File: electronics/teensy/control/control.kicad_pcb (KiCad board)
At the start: 2 copper layers, 100 x 100 mm, 154 parts, among them J1 Vin 24V, J10 Z_MAX, J11 OTHER_2, J12 Stepper X1, J13 Stepper X2, J14 Stepper X1, J15 Stepper X1, J16 DC Motor Vin 24V, J18 DC Motor, J2 Vout 5V, J20 DC Motor Vin 24V, J21 DC Motor, J22 SPINDLE_BLDC_CONTROLLER, J23 USB_B, J24 EXT, J25 EXT, J3 Vout 3.3V, J4 X_MIN, J5 Y_MIN, J6 Z_MIN, J7 OTHER 1, J8 X_MAX, J9 Y_MAX, Q1 TK1R4S04PB, Q3 TK1R4S04PB, Q4 SI2301CDS-T1-E3, U1 MIC4684, U10 MOCD217R2M, U11 MOCD217R2M, U12 MOCD217R2M, U13 MOCD217R2M, U14 TS912, U15 MOCD217R2M, U16 Cetus_J1B1211CCD, U17 CY7C64225, U18 LM810M3-4.63, U19 Teensy_4.1, U2 AP7354-33W5-7, U3 AZ1117IH-3.3TRG1, U4 SN74LVC14ADRG3, U5 SN74LVC14ADRG3, U6 MOCD217R2M, U7 MOCD217R2M, U8 MOCD217R2M, U9 MOCD217R2M

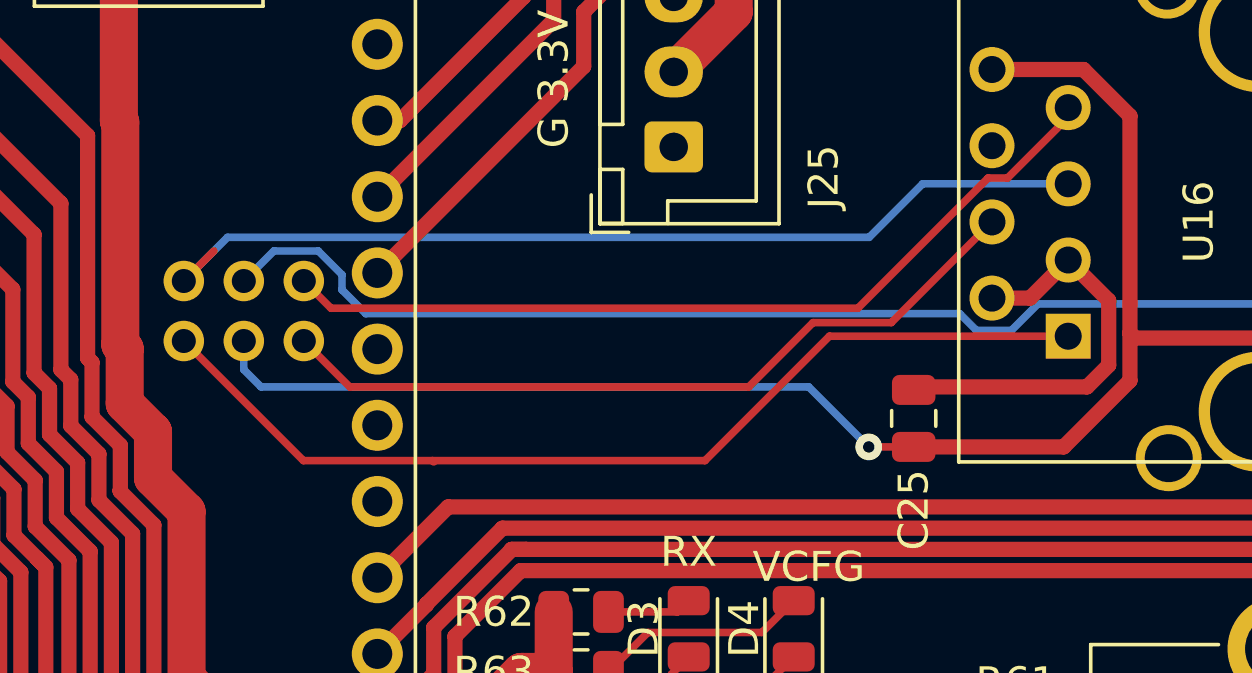
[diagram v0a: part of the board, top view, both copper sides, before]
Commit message: Add core classes and functions.
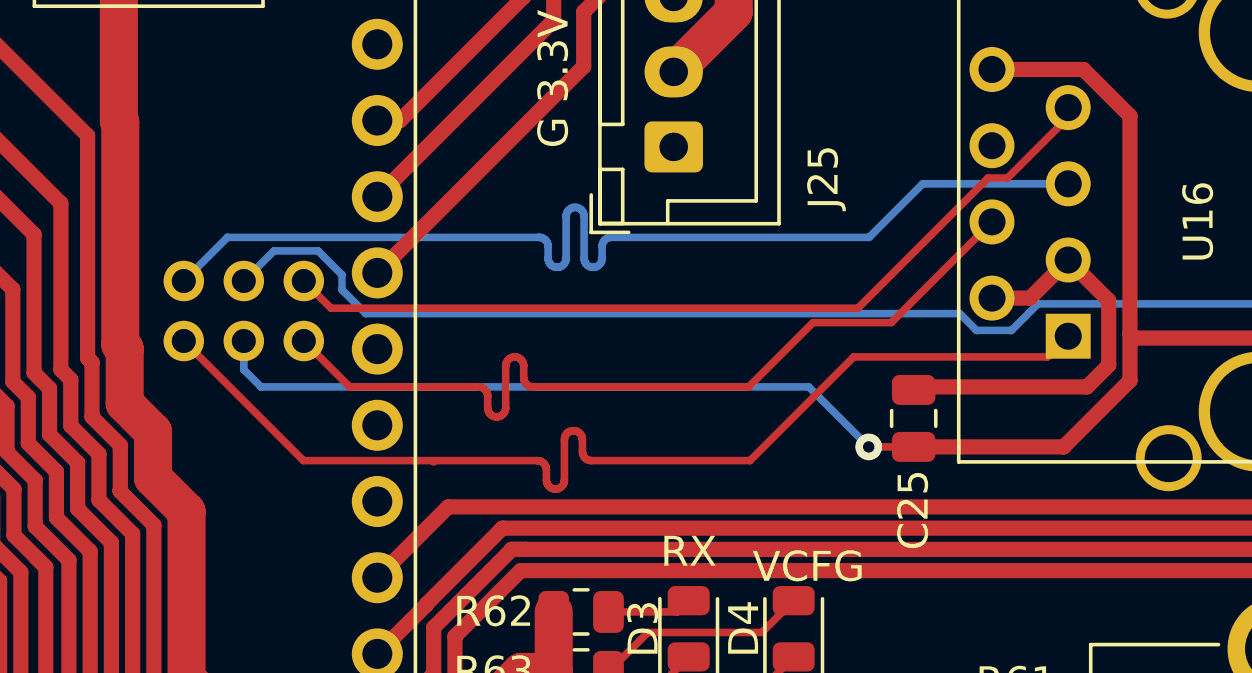
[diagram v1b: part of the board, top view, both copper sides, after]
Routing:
- net /mcu/ETH_TX-: track 32.2 -> 35.8 mm
- net /mcu/ETH_RX-: track 25.9 -> 29.1 mm
- net /mcu/ETH_TX+: track 32.9 -> 36.0 mm

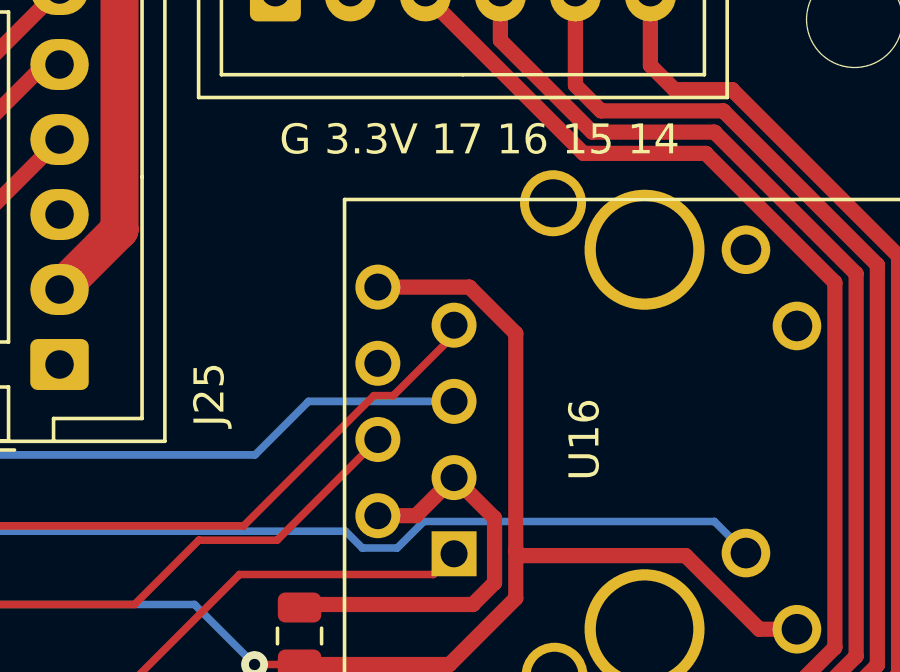
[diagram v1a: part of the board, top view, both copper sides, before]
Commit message: Add ResourceLock tests.
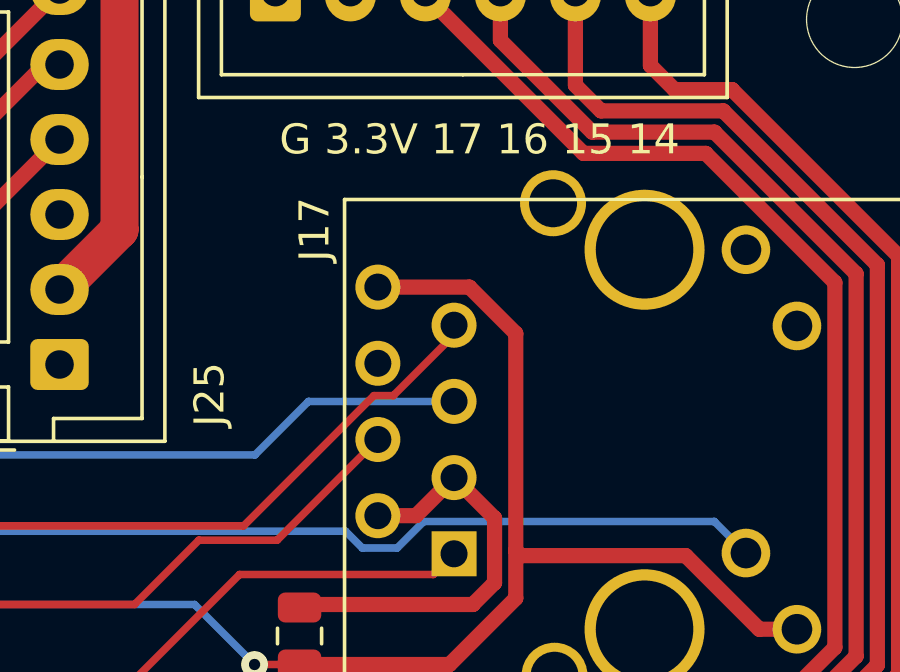
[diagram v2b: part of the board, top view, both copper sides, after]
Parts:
- renumbered U16 to J17

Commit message: Add gerber files
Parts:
- added R44: 20k, Resistor_SMD:R_0805_2012Metric, F.Cu at (100.9, 68.0)
- added R49: 1k, Resistor_SMD:R_0805_2012Metric, F.Cu at (86.0, 70.9)
- added R50: 1k, Resistor_SMD:R_0805_2012Metric, F.Cu at (83.6, 60.0)
- added R69: 1k, Resistor_SMD:R_0805_2012Metric, F.Cu at (83.6, 63.5)
- added R70: 1k, Resistor_SMD:R_0805_2012Metric, F.Cu at (83.0, 70.9)
- added R71: 1k, Resistor_SMD:R_0805_2012Metric, F.Cu at (97.0, 51.6)
- R59: value 1k -> 10k
- moved R59 1.00 mm to (100.9, 65.0)
- moved R60 1.00 mm to (100.9, 62.0)
- moved R61 1.00 mm to (100.9, 56.0)
- moved J17 0.50 mm to (109.0, 37.5)
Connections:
- U17 pad 21: /mcu/USB_UART_CTS -> Net-(R69-Pad2)
- U17 pad 22: /mcu/USB_UART_WAKE -> Net-(R71-Pad1)
- U17 pad 23: /mcu/USB_UART_RX -> Net-(R70-Pad2)
- U17 pad 24: /mcu/USB_UART_RTS -> Net-(R50-Pad2)
- U17 pad 4: /mcu/USB_UART_TX -> Net-(R49-Pad2)
- U17 pad 5: /mcu/USB_UART_DTR -> Net-(U17-Pad5)
- U17 pad 6: /mcu/USB_UART_RESET -> Net-(U17-Pad6)
- U17 pad 8: /mcu/USB_UART_DSR -> Net-(U17-Pad5)
- U19 pad 36: /mcu/USB_UART_DTR -> Net-(U19-Pad36)
- U19 pad 37: /mcu/USB_UART_RESET -> Net-(U19-Pad37)
- U19 pad 38: /mcu/USB_UART_DSR -> Net-(U19-Pad38)
- U19 pad 40: /mcu/USB_UART_WAKE -> Net-(U19-Pad40)
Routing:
- net /mcu/USB_UART_DSR: track 26.9 -> 0.00 mm
- net /mcu/USB_UART_DTR: track 26.9 -> 0.00 mm
- net /mcu/USB_UART_RESET: track 26.6 -> 0.00 mm
- net /mcu/USB_UART_RX: track 33.2 -> 9.92 mm, vias 1 -> 0
- net /mcu/USB_UART_WAKE: track 19.5 -> 0.00 mm
- net Net-(R70-Pad2): track 0.00 -> 18.3 mm
- net /mcu/USB_UART_TX: track 28.6 -> 13.7 mm
- net /mcu/ETH_LED: track 39.8 -> 54.6 mm
- net /mcu/USB_UART_CTS: track 22.3 -> 7.95 mm
- net Net-(R49-Pad2): track 0.00 -> 13.5 mm
- net Net-(R69-Pad2): track 0.00 -> 13.1 mm, vias 0 -> 2
- net /mcu/USB_UART_RTS: track 17.1 -> 7.05 mm
- net Net-(R50-Pad2): track 0.00 -> 9.39 mm
- net Net-(R71-Pad1): track 0.00 -> 6.13 mm
- net Net-(U17-Pad5): track 0.00 -> 4.51 mm
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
